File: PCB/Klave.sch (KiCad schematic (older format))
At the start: 83 parts, among them J1 TRRS, J2 OLED, SW0 SW_Reset, SW1 SW_Key, SW10 SW_Key, SW11 SW_Key, SW12 SW_Key, SW13 SW_Key, SW14 SW_Key, SW15 SW_Key, SW16 SW_Key, SW17 SW_Key, SW18 SW_Key, SW19 SW_Key, SW2 SW_Key, SW20 SW_Key, SW21 SW_Key, SW22 SW_Key, SW23 SW_Key, SW24 SW_Key, SW26 SW_Key, SW27 SW_Key, SW28 SW_Key, SW29 SW_Key, SW3 SW_Key, SW30 SW_Key, SW35 SW_Key, SW36 SW_Key, SW4 SW_Key, SW5 SW_Key, SW6 SW_Key, SW7 SW_Key, SW8 SW_Key, SW9 SW_Key, U1 ProMicro

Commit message: Remove TRRS connector
Will be replaced with RJ11 or similar connector.
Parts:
- removed J1: TRRS, symbol KlaveLib:TRRS
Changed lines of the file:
@@
 	-1   0    0    1
-$EndComp
-$Comp
-L KlaveLib:TRRS J1
-U 1 1 5F439991
-P 1300 5500
-F 0 "J1" H 1382 5917 50  0000 C CNN
-F 1 "TRRS" H 1382 5826 50  0000 C CNN
-F 2 "" H 1350 5600 50  0001 C CNN
-F 3 "" H 1350 5600 50  0001 C CNN
-	1    1300 5500
-	1    0    0    -1
 $EndComp
 Text GLabel 1050 1850 0    50   Input ~ 0

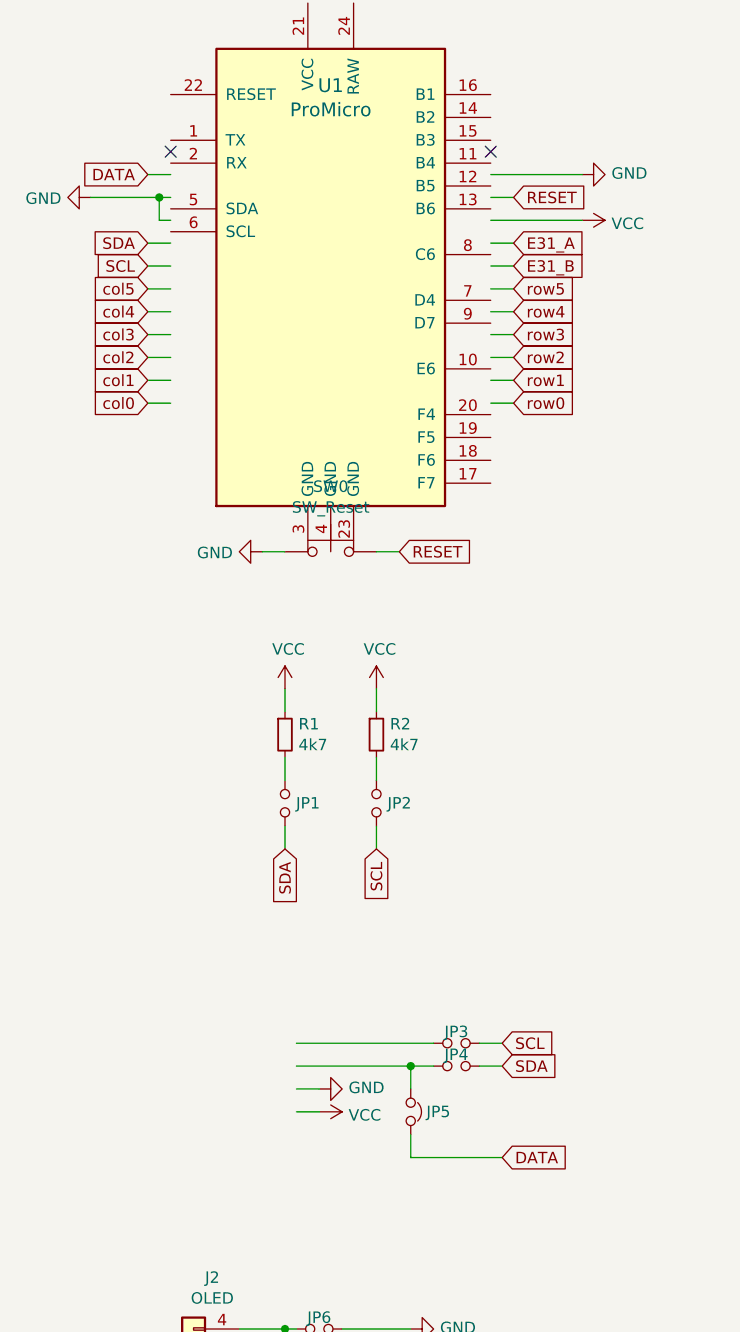
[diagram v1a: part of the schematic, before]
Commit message: Drop serial communication support
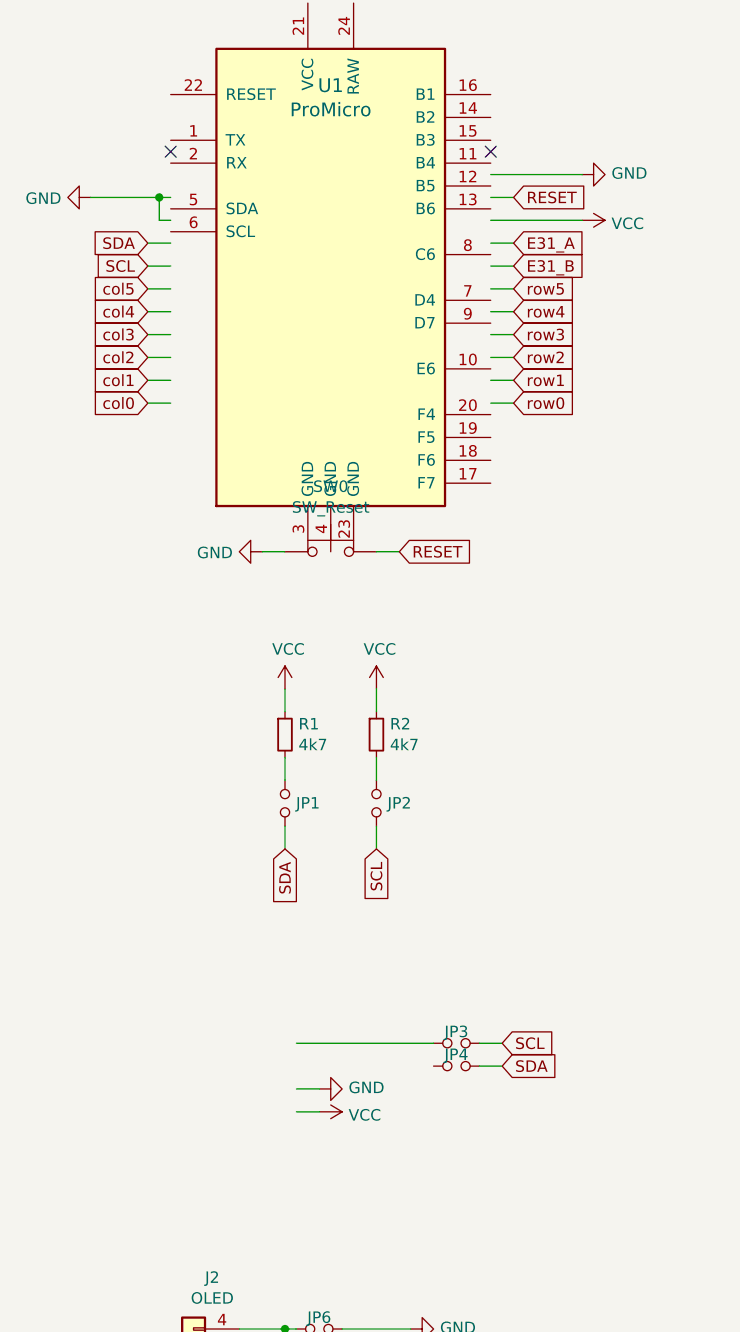
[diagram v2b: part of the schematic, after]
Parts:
- removed JP5: Jumper_Serial, symbol Device:Jumper_NC_Small
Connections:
- net labels removed: DATA
- wire segments 202 -> 196
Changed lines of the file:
@@
 	0    -1   -1   0
 $EndComp
-Text GLabel 1050 1550 0    50   Input ~ 0
-DATA
 $Comp
 L Switch:SW_Push SW0
@@
 	1050 1950 1150 1950
 Wire Wire Line
-	1050 1550 1150 1550
-Wire Wire Line
 	2550 1750 2950 1750
 Wire Wire Line
@@
 $EndComp
 Wire Wire Line
-	1700 5450 2200 5450
-Connection ~ 2200 5450
-Wire Wire Line
-	2200 5450 2300 5450
-Wire Wire Line
 	2300 5350 1700 5350
 Wire Wire Line
@@
 Wire Wire Line
 	2500 5450 2600 5450
-Wire Wire Line
-	2200 5550 2200 5450
-Text GLabel 2600 5850 2    50   Input ~ 0
-DATA
-$Comp
-L Device:Jumper_NC_Small JP5
-U 1 1 5F4951D7
-P 2200 5650
-F 0 "JP5" V 2200 5771 50  0000 C CNN
-F 1 "Jumper_Serial" H 2200 5771 50  0001 C CNN
-F 2 "" H 2200 5650 50  0001 C CNN
-F 3 "~" H 2200 5650 50  0001 C CNN
-	1    2200 5650
-	0    1    1    0
-$EndComp
-Wire Wire Line
-	2200 5750 2200 5850
-Wire Wire Line
-	2200 5850 2600 5850
 $Comp
 L Device:Jumper_NO_Small JP2

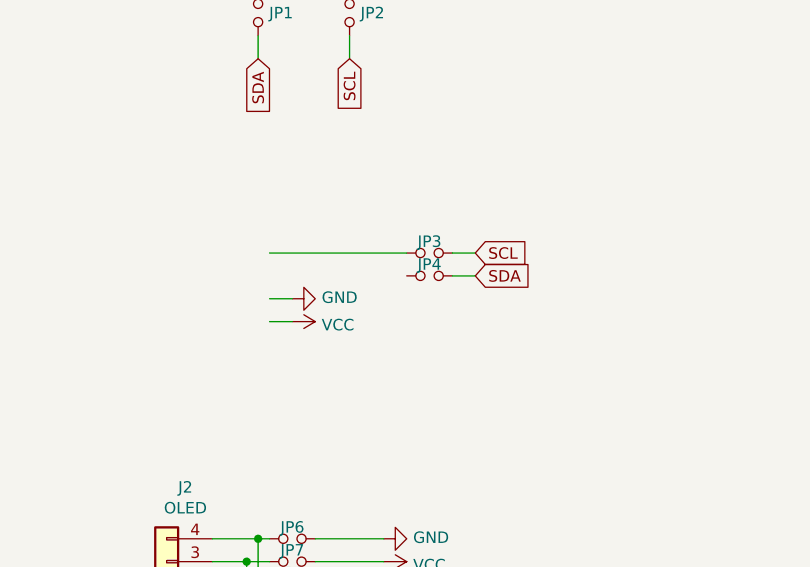
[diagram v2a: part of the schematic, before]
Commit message: Remove connector from schematic
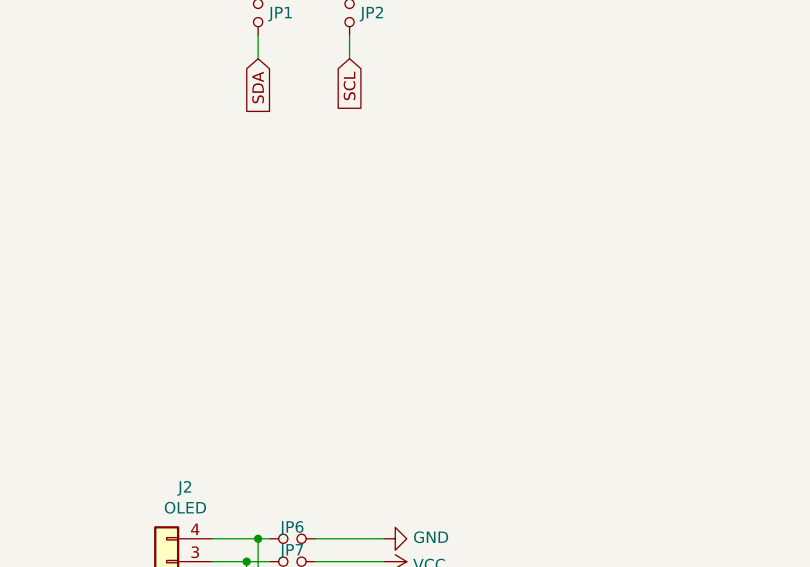
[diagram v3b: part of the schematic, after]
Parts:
- removed JP3, JP4: Jumper_I2C, symbol Device:Jumper_NO_Small
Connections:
- wire segments 196 -> 191
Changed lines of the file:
@@
 Wire Wire Line
 	1100 1650 1150 1650
-$Comp
-L power:VCC #PWR0104
-U 1 1 5F4571D6
-P 1800 5650
-F 0 "#PWR0104" H 1800 5500 50  0001 C CNN
-F 1 "VCC" V 1815 5778 50  0000 L CNN
-F 2 "" H 1800 5650 50  0001 C CNN
-F 3 "" H 1800 5650 50  0001 C CNN
-	1    1800 5650
-	0    1    1    0
-$EndComp
-Text GLabel 2600 5450 2    50   Input ~ 0
-SDA
 Text GLabel 1050 1950 0    50   Input ~ 0
 SCL
-Text GLabel 2600 5350 2    50   Input ~ 0
-SCL
-$Comp
-L power:GND #PWR0105
-U 1 1 5F458287
-P 1800 5550
-F 0 "#PWR0105" H 1800 5300 50  0001 C CNN
-F 1 "GND" V 1805 5422 50  0000 R CNN
-F 2 "" H 1800 5550 50  0001 C CNN
-F 3 "" H 1800 5550 50  0001 C CNN
-	1    1800 5550
-	0    -1   -1   0
-$EndComp
 Text GLabel 2000 6800 2    50   Input ~ 0
 SCL
@@
 RESET
 Wire Wire Line
-	1700 5550 1800 5550
-Wire Wire Line
 	2050 3200 2150 3200
 Wire Wire Line
@@
 Wire Wire Line
 	2550 1550 2950 1550
-Wire Wire Line
-	1700 5650 1800 5650
 $Comp
 L Device:Jumper_NO_Small JP6
@@
 	2050 3800 2050 3900
 $Comp
-L Device:Jumper_NO_Small JP3
-U 1 1 5F48CDA7
-P 2400 5350
-F 0 "JP3" H 2400 5400 50  0000 C CNN
-F 1 "Jumper_I2C" H 2400 5444 50  0001 C CNN
-F 2 "" H 2400 5350 50  0001 C CNN
-F 3 "~" H 2400 5350 50  0001 C CNN
-	1    2400 5350
-	1    0    0    -1
-$EndComp
-$Comp
-L Device:Jumper_NO_Small JP4
-U 1 1 5F494913
-P 2400 5450
-F 0 "JP4" H 2400 5500 50  0000 C CNN
-F 1 "Jumper_I2C" H 2400 5544 50  0001 C CNN
-F 2 "" H 2400 5450 50  0001 C CNN
-F 3 "~" H 2400 5450 50  0001 C CNN
-	1    2400 5450
-	1    0    0    -1
-$EndComp
-Wire Wire Line
-	2300 5350 1700 5350
-Wire Wire Line
-	2500 5350 2600 5350
-Wire Wire Line
-	2500 5450 2600 5450
-$Comp
 L Device:Jumper_NO_Small JP2

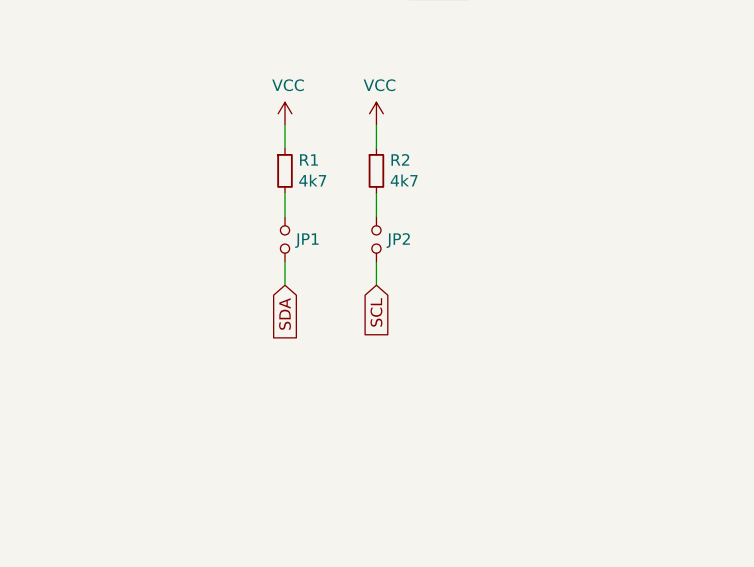
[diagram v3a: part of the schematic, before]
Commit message: Remove I2C pull-up resistor jumpers
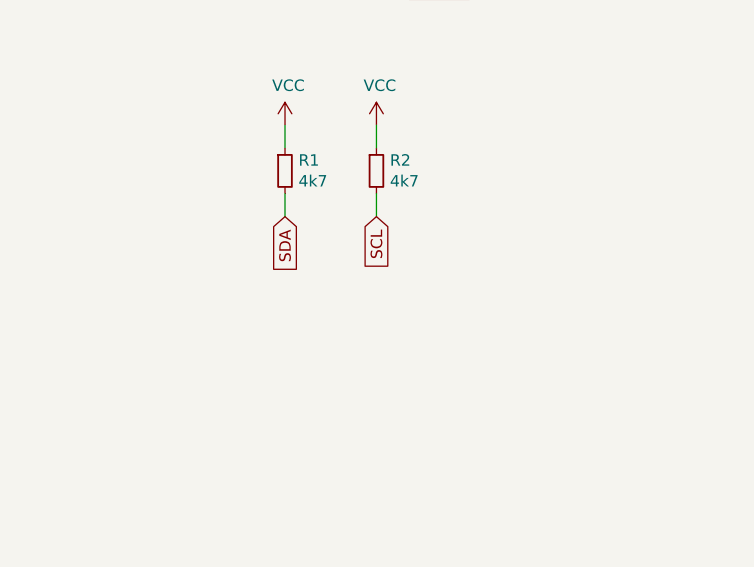
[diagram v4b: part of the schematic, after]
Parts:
- removed JP1, JP2: Jumper_Master, symbol Device:Jumper_NO_Small
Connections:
- wire segments 191 -> 189
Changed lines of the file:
@@
 	1    0    0    -1
 $EndComp
-Text GLabel 1650 4500 3    50   Input ~ 0
+Text GLabel 1650 4200 3    50   Input ~ 0
 SDA
-Text GLabel 2050 4500 3    50   Input ~ 0
+Text GLabel 2050 4200 3    50   Input ~ 0
 SCL
 $Comp
@@
 Wire Wire Line
 	2050 3800 2050 3900
-$Comp
-L Device:Jumper_NO_Small JP2
-U 1 1 5F4B31FD
-P 2050 4300
-F 0 "JP2" V 2050 4252 50  0000 R CNN
-F 1 "Jumper_Master" V 2005 4252 50  0001 R CNN
-F 2 "" H 2050 4300 50  0001 C CNN
-F 3 "~" H 2050 4300 50  0001 C CNN
-	1    2050 4300
-	0    -1   -1   0
-$EndComp
-$Comp
-L Device:Jumper_NO_Small JP1
-U 1 1 5F4B5EF6
-P 1650 4300
-F 0 "JP1" V 1650 4252 50  0000 R CNN
-F 1 "Jumper_Master" V 1605 4252 50  0001 R CNN
-F 2 "" H 1650 4300 50  0001 C CNN
-F 3 "~" H 1650 4300 50  0001 C CNN
-	1    1650 4300
-	0    -1   -1   0
-$EndComp
 Wire Wire Line
 	2050 4100 2050 4200
-Wire Wire Line
-	2050 4400 2050 4500
-Wire Wire Line
-	1650 4400 1650 4500
 $Comp
 L power:PWR_FLAG #FLG0101

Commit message: Remake ProMicro schematic symbol
Reorder pins to functional pin order.
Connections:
- net labels added: encA, encB
- net labels removed: E31_A, E31_B
- wire segments 189 -> 190
- no-connect marks 2 -> 3
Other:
- moved on the sheet: J2, JP10, JP11, JP12, JP13, JP6, JP7, JP8, JP9, R1, R2, SW0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

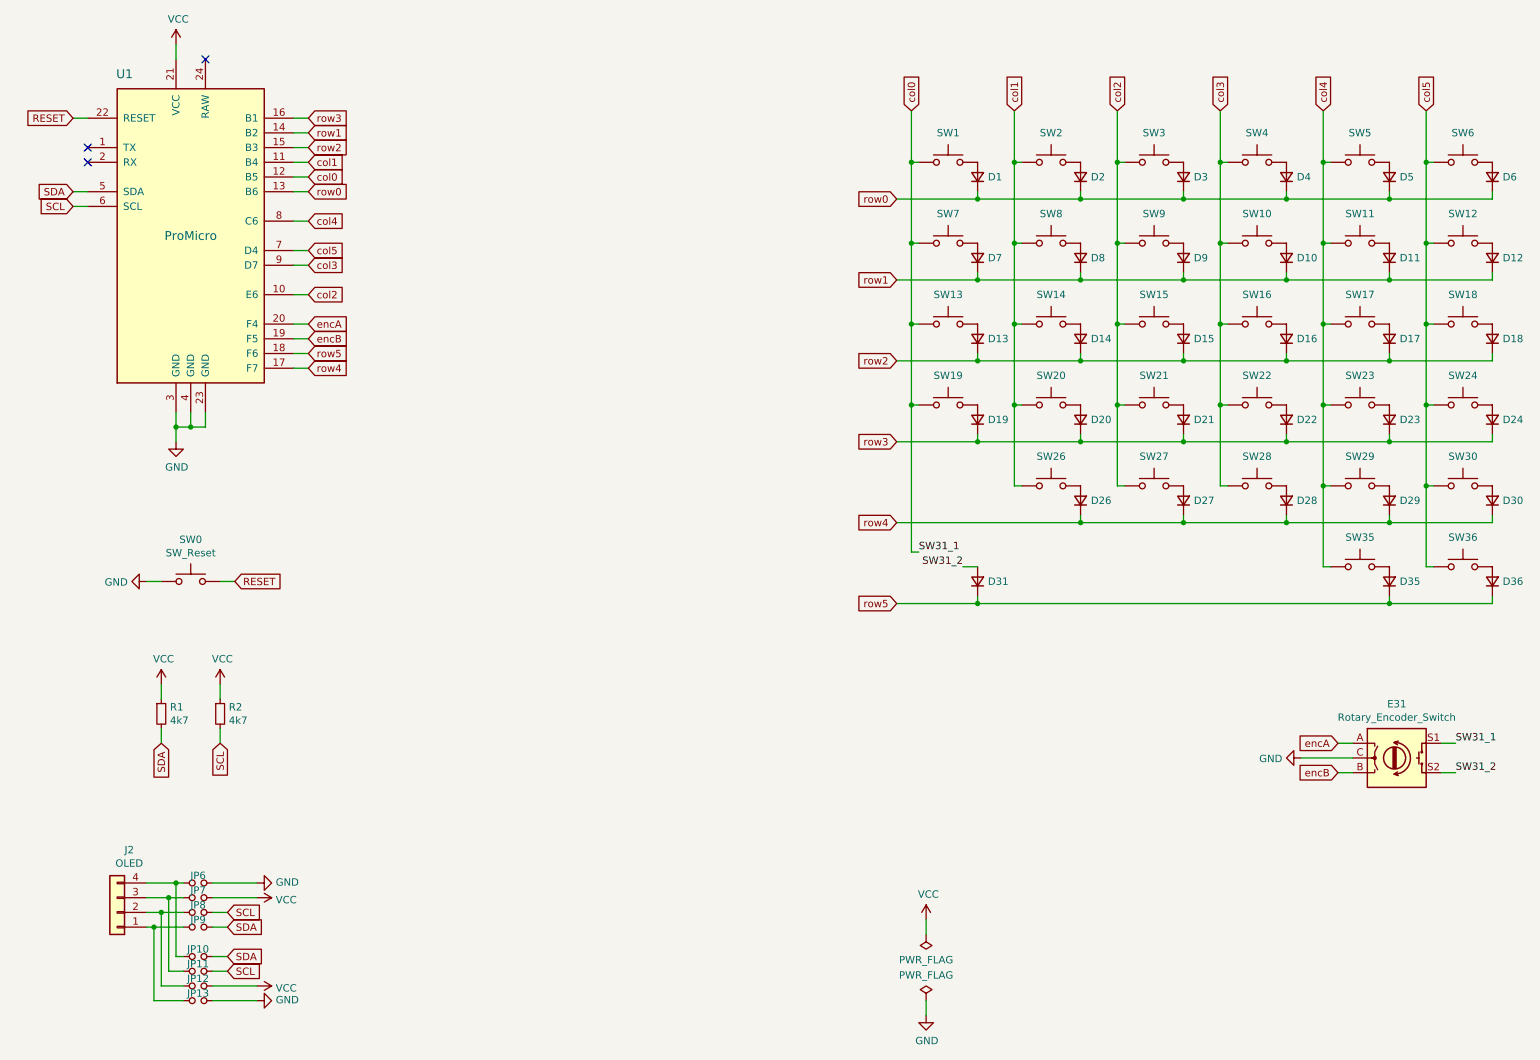
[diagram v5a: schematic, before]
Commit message: Set schematic symbols values
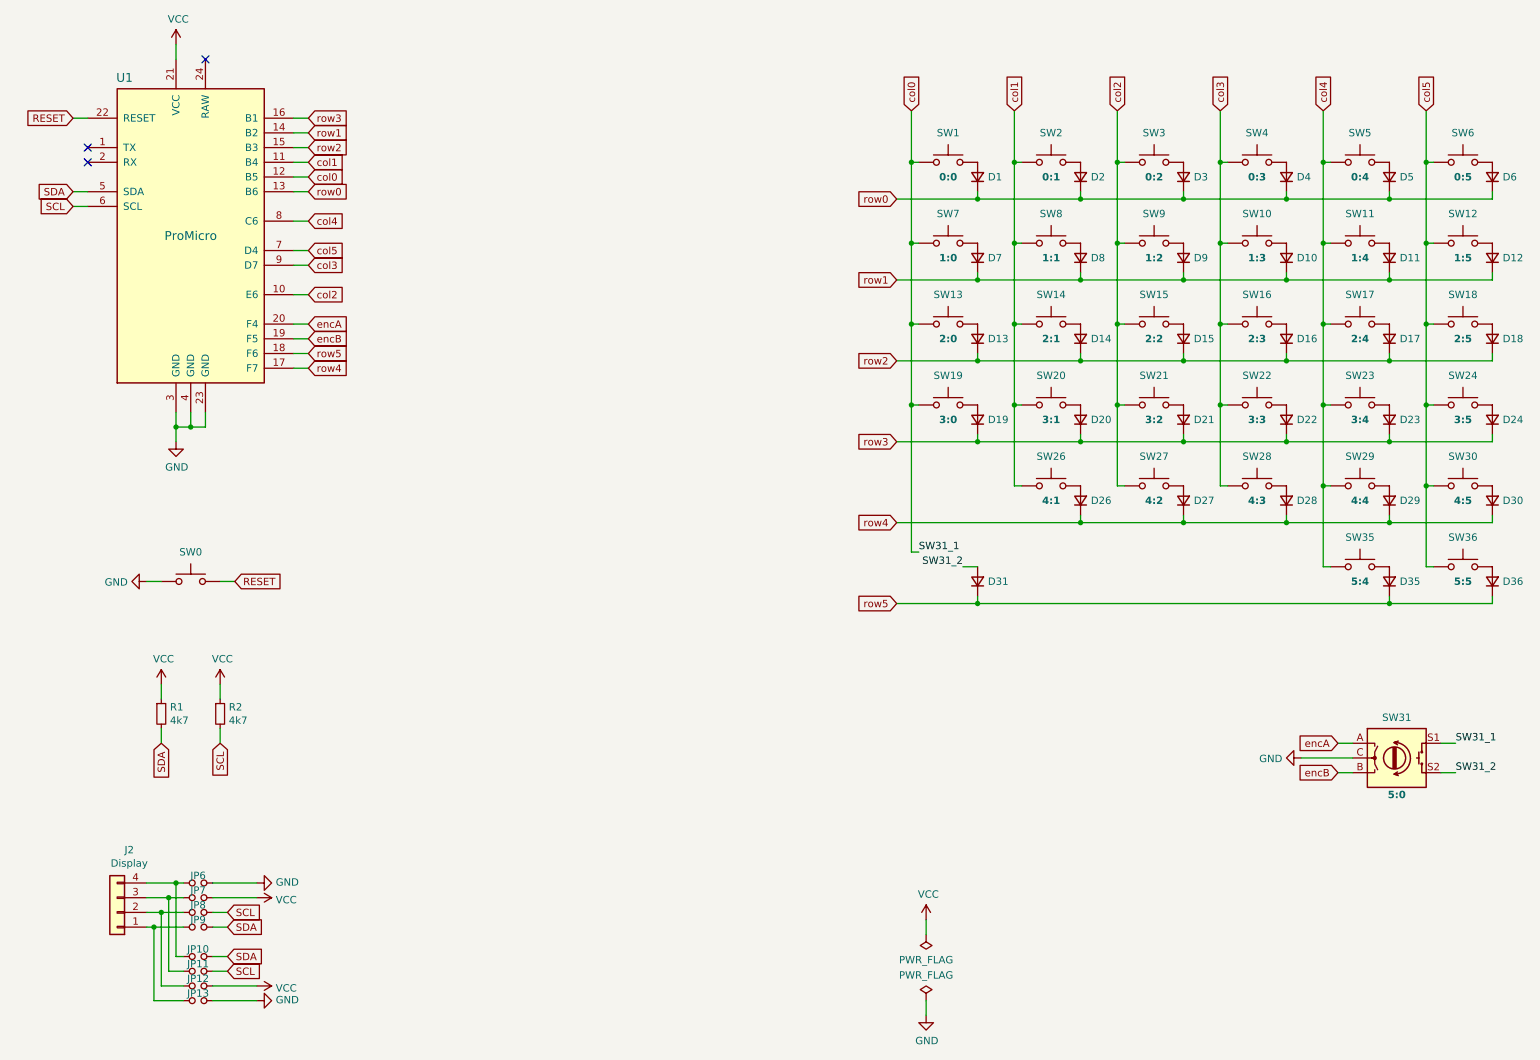
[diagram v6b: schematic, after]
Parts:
- D1: value D_Key -> 0:0
- D10: value D_Key -> 1:3
- D11: value D_Key -> 1:4
- D12: value D_Key -> 1:5
- D13: value D_Key -> 2:0
- D14: value D_Key -> 2:1
- D15: value D_Key -> 2:2
- D16: value D_Key -> 2:3
- D17: value D_Key -> 2:4
- D18: value D_Key -> 2:5
- D19: value D_Key -> 3:0
- D2: value D_Key -> 0:1
- D20: value D_Key -> 3:1
- D21: value D_Key -> 3:2
- D22: value D_Key -> 3:3
- D23: value D_Key -> 3:4
- D24: value D_Key -> 3:5
- D26: value D_Key -> 4:1
- D27: value D_Key -> 4:2
- D28: value D_Key -> 4:3
- D29: value D_Key -> 4:4
- D3: value D_Key -> 0:2
- D30: value D_Key -> 4:5
- D31: value D_Key -> 5:0
- D35: value D_Key -> 5:4
- D36: value D_Key -> 5:5
- D4: value D_Key -> 0:3
- D5: value D_Key -> 0:4
- D6: value D_Key -> 0:5
- D7: value D_Key -> 1:0
- D8: value D_Key -> 1:1
- D9: value D_Key -> 1:2
- J2: value OLED -> Display
- JP10, JP11, JP12, JP13: value Jumper_Back -> Back
- JP6, JP7, JP8, JP9: value Jumper_Front -> Front
- SW0: value SW_Reset -> Reset
- SW1: value SW_Key -> 0:0
- SW10: value SW_Key -> 1:3
- SW11: value SW_Key -> 1:4
- SW12: value SW_Key -> 1:5
- SW13: value SW_Key -> 2:0
- SW14: value SW_Key -> 2:1
- SW15: value SW_Key -> 2:2
- SW16: value SW_Key -> 2:3
- SW17: value SW_Key -> 2:4
- SW18: value SW_Key -> 2:5
- SW19: value SW_Key -> 3:0
- SW2: value SW_Key -> 0:1
- SW20: value SW_Key -> 3:1
- SW21: value SW_Key -> 3:2
- SW22: value SW_Key -> 3:3
- SW23: value SW_Key -> 3:4
- SW24: value SW_Key -> 3:5
- SW26: value SW_Key -> 4:1
- SW27: value SW_Key -> 4:2
- SW28: value SW_Key -> 4:3
- SW29: value SW_Key -> 4:4
- SW3: value SW_Key -> 0:2
- SW30: value SW_Key -> 4:5
- SW31: renamed from E31; value Rotary_Encoder_Switch -> 5:0
- SW35: value SW_Key -> 5:4
- SW36: value SW_Key -> 5:5
- SW4: value SW_Key -> 0:3
- SW5: value SW_Key -> 0:4
- SW6: value SW_Key -> 0:5
- SW7: value SW_Key -> 1:0
- SW8: value SW_Key -> 1:1
- SW9: value SW_Key -> 1:2

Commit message: Assign PCB footprints to schematic symbols
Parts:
- D1, D10, D11, D12, D13, D14, D15, D16, D17, D18, D19, D2, D20, D21, D22, D23, D24, D26, D27, D28, D29, D3, D30, D31, D35, D36, D4, D5, D6, D7, D8, D9: footprint (none) -> KlaveLib:D_SOD-123
- J2: footprint (none) -> KlaveLib:Display_OLED_128x32
- JP10, JP11, JP12, JP13, JP6, JP7, JP8, JP9: footprint (none) -> Jumper:SolderJumper-2_P1.3mm_Open_Pad1.0x1.5mm
- R1, R2: footprint (none) -> KlaveLib:R_Axial_DIN0207_L6.3mm_D2.5mm_P10.16mm_Horizontal
- SW0: footprint (none) -> KlaveLib:SW_Tactile_2pin
- SW1, SW10, SW11, SW12, SW13, SW14, SW15, SW16, SW17, SW18, SW19, SW2, SW20, SW21, SW22, SW23, SW24, SW26, SW27, SW28, SW29, SW3, SW30, SW35, SW36, SW4, SW5, SW6, SW7, SW8, SW9: footprint (none) -> KlaveLib:Kailh_MX_Socket
- SW31: footprint (none) -> KlaveLib:RotaryEncoder_EC11E-Switch
- U1: footprint (none) -> KlaveLib:Arduino_ProMicro
